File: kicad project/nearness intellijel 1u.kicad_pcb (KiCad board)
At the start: 2 copper layers, 70.8 x 22.5 mm, 48 parts, among them J1 PJ301M12, J10 PJ301M12, J2 PJ301M12, J3 PJ301M12, J4 PJ301M12, J5 PJ301M12, J6 PJ301M12, J7 PJ301M12, J8 PJ301M12, J9 PJ301M12, P1 CONN_01X03, P7 CONN_01X03, U1 TL072, U2 TL072

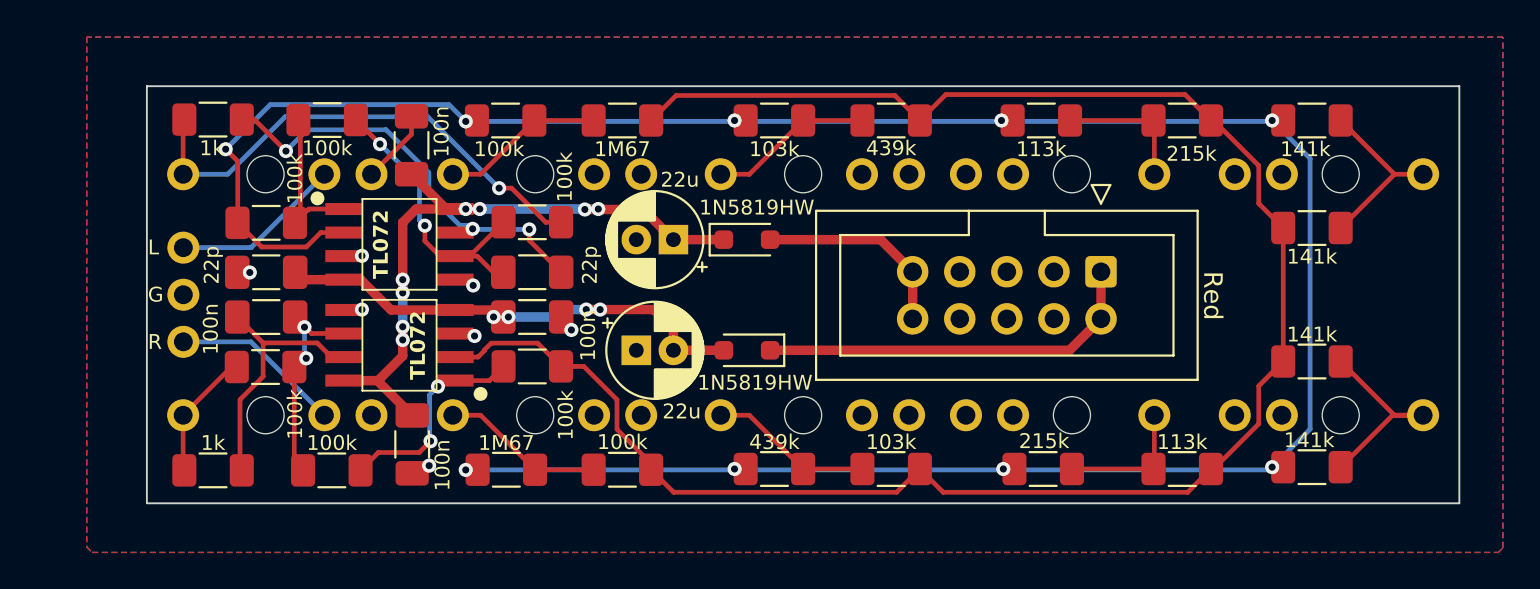
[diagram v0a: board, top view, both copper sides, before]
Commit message: Adjusted resistor values
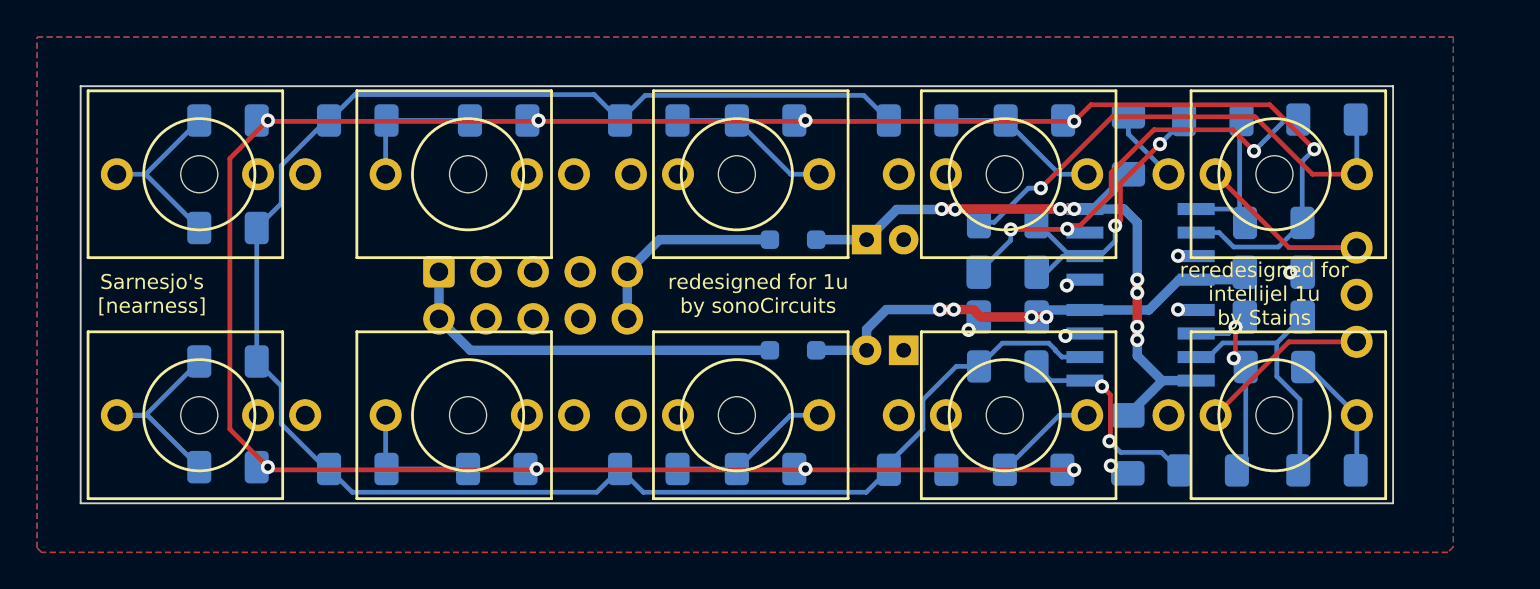
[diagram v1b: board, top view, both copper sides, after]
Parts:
- C1, C2, C3, C4, C5, C6, C7, C8, P1, P7, R1, R10, R14, R15, R17, R19, R20, R21, R22, R23, R24, R5, R6, R9, U1, U2: moved to B.Cu
- D1, D2: value 1N5819HW -> Schottky; moved to B.Cu
- J1, J10, J2, J3, J4, J5, J6, J7, J8, J9: moved to F.Cu
- R11, R4: value 439k -> 442k; moved to B.Cu
- R12, R3: value 103k -> 102k; moved to B.Cu
- R13, R2: value 1M67 -> 1M65; moved to B.Cu
- R25, R26, R7, R8: value 141k -> 140k; moved to B.Cu
- moved P1 63.3 mm to (165.1, 132.8), turned to 180 degrees
- moved J10 61.6 mm to (102.7, 126.3)
- moved J5 61.6 mm to (102.7, 139.3)
- moved R23 60.1 mm to (163.5, 123.4), turned to 0 degrees
- moved R24 60.1 mm to (163.5, 142.3), turned to 0 degrees
- moved R25 58.5 mm to (104.2, 123.4), turned to 0 degrees
- moved R26 58.5 mm to (104.2, 129.2), turned to 0 degrees
- moved R7 58.5 mm to (104.2, 142.1), turned to 0 degrees
- moved R8 58.5 mm to (104.2, 136.4), turned to 0 degrees
- moved J1 54.4 mm to (160.7, 126.3)
- moved J9 54.4 mm to (160.7, 139.3)
- moved R22 54.4 mm to (160.7, 136.7), turned to 0 degrees
- moved C2 54.4 mm to (160.6, 134.0), turned to 0 degrees
- moved C8 54.4 mm to (160.6, 131.6), turned to 180 degrees
- moved R15 54.4 mm to (160.6, 129.0), turned to 180 degrees
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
